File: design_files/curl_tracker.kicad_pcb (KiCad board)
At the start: 2 copper layers, 38 parts, among them J1 JST-PH, J2 USB_C_Receptacle, J3 SSD1306 OLED, J4 JST-PH, Q1 DMP2035, Q2 AO3400A, SW1 SW_Push, SW2 SW_Push, SW3 SW_Push, U1 AP2112K-3.3, U2 ESP32-C3-MINI-1, U3 MCP73831-2-OT, U4 BMI270, U5 USBLC6-2SC6

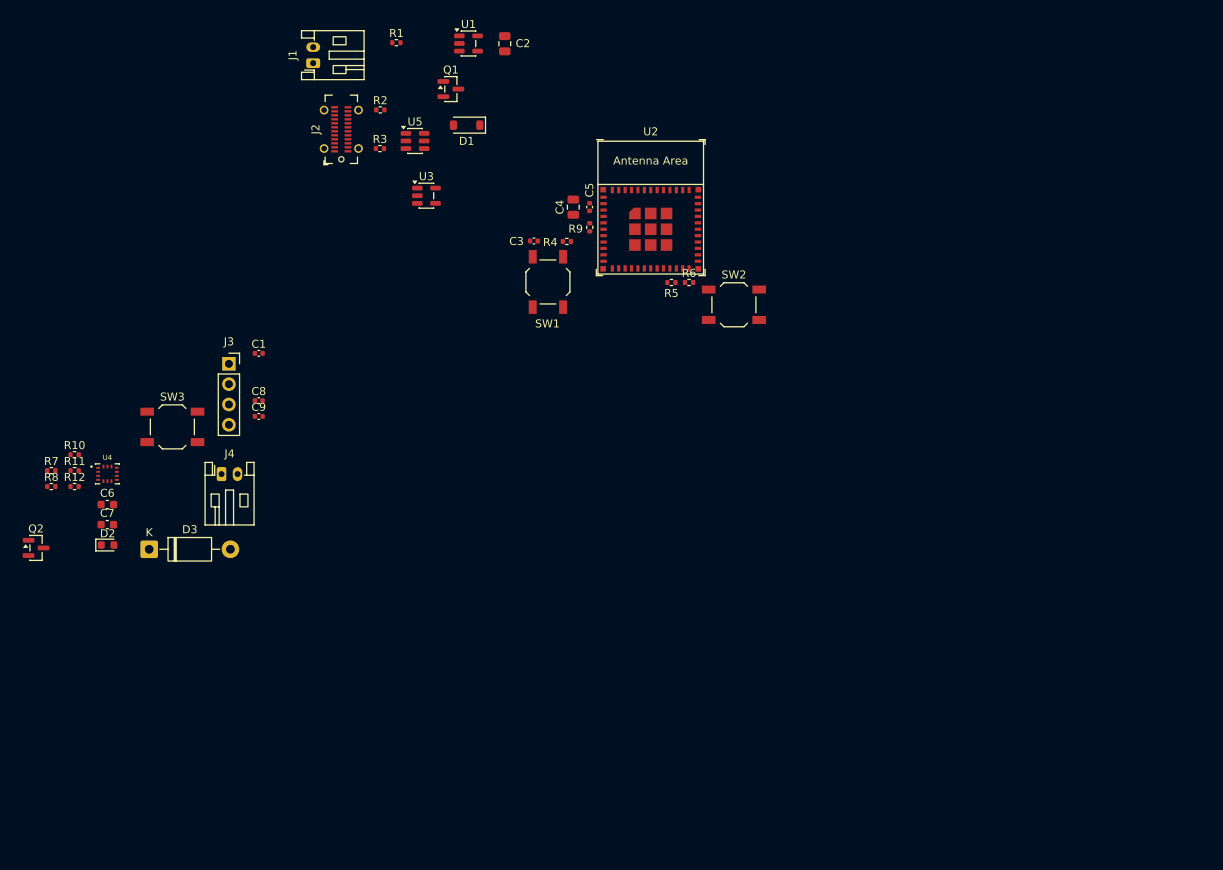
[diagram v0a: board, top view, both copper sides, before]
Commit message: start of esp-idf transition
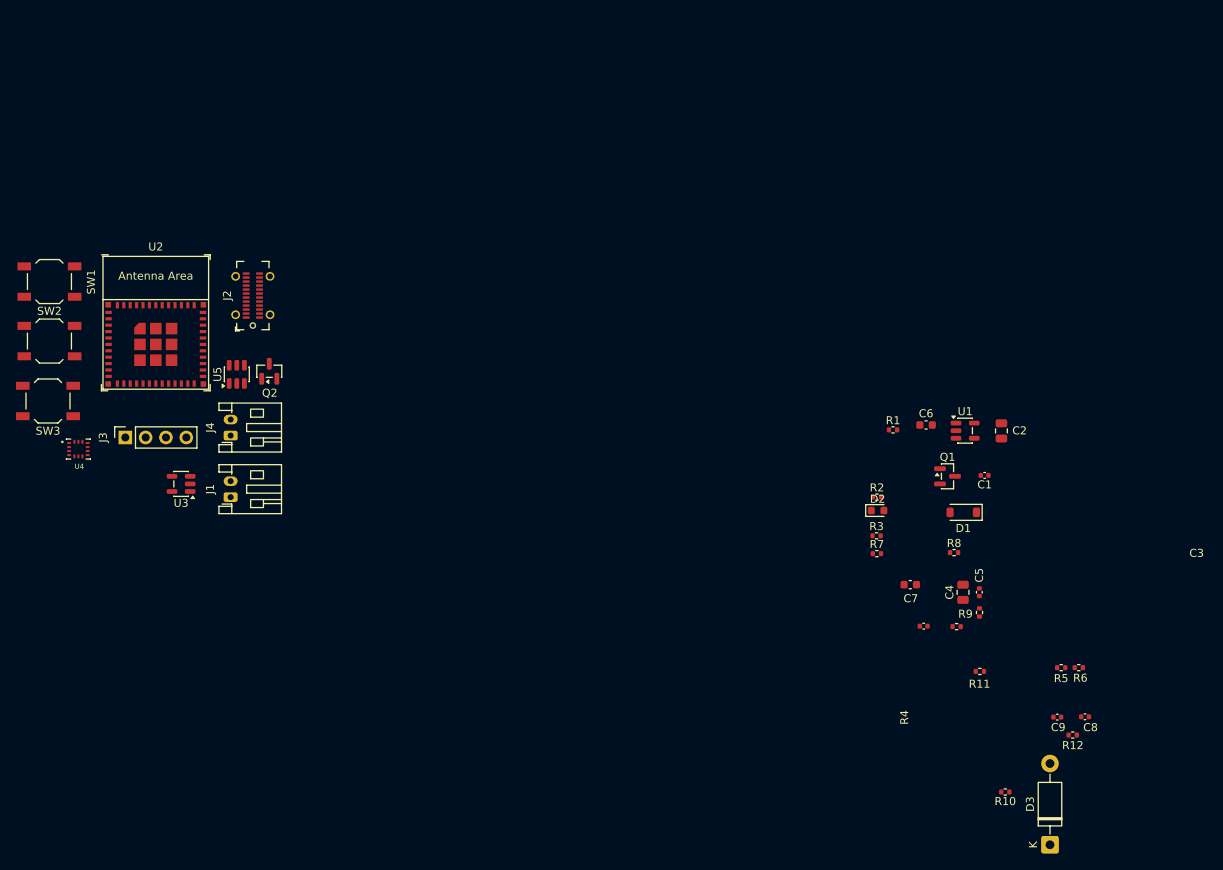
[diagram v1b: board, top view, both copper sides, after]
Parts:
- moved R12 128.6 mm to (255.7, 134.6)
- moved R10 123.7 mm to (247.2, 141.7), turned to 180 degrees
- moved D3 118.5 mm to (252.8, 148.3), turned to 90 degrees
- moved R11 115.9 mm to (244.0, 126.7)
- moved R8 113.1 mm to (240.8, 111.8)
- moved C8 110.6 mm to (257.2, 132.3), turned to 180 degrees
- moved C9 106.7 mm to (253.7, 132.4)
- moved R7 103.7 mm to (231.2, 111.9)
- moved C6 102.8 mm to (237.3, 95.9)
- moved C7 100.7 mm to (235.3, 115.8)
- moved D2 96.3 mm to (231.3, 106.5)
- moved C1 92.0 mm to (244.6, 102.2), turned to 180 degrees
- moved SW2 85.7 mm to (127.7, 85.4)
- moved D1 78.7 mm to (242.0, 106.8)
- moved Q1 78.7 mm to (240.0, 102.3)
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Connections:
- J3 pad 1: GND -> +3.3V
- J3 pad 2: +3.3V -> GND

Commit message: finished schematic
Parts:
- added C10: 4.7uF, Capacitor_SMD:C_0805_2012Metric, F.Cu at (158.7, 100.3)
- added C11: 4.7uF, Capacitor_SMD:C_0805_2012Metric, F.Cu at (163.1, 94.3)
- added C12: 100nF, Capacitor_SMD:C_0402_1005Metric, F.Cu at (140.3, 110.1)
- added C13: 100nF, Capacitor_SMD:C_0805_2012Metric, F.Cu at (163.1, 97.3)
- added C14: 100nF, Capacitor_SMD:C_0805_2012Metric, F.Cu at (163.1, 100.3)
- added C15: 100nF, Capacitor_SMD:C_0402_1005Metric, F.Cu at (140.3, 112.1)
- added L1: 2.2uH, Inductor_SMD:L_Coilcraft_LPS4018, F.Cu at (161.8, 118.7)
- added R13: 5.1k, Resistor_SMD:R_0402_1005Metric, F.Cu at (147.6, 103.7)
- added R14: 5.1k, Resistor_SMD:R_0402_1005Metric, F.Cu at (147.6, 105.7)
- added R15: 470, Resistor_SMD:R_0402_1005Metric, F.Cu at (150.5, 93.8)
- added R16: 5k, Resistor_SMD:R_0402_1005Metric, F.Cu at (150.5, 95.8)
- added R17: 10k, Resistor_SMD:R_0402_1005Metric, F.Cu at (150.5, 97.8)
- added R18: 100, Resistor_SMD:R_0402_1005Metric, F.Cu at (150.5, 99.7)
- added R19: 10k, Resistor_SMD:R_0402_1005Metric, F.Cu at (150.5, 101.7)
- C1, C3: value 1uF -> 10uF; footprint Capacitor_SMD:C_0402_1005Metric -> Capacitor_SMD:C_0805_2012Metric
- C5: value 100nF -> 1uF
- C6: value 4.7uF -> 100nF; footprint Capacitor_SMD:C_0603_1608Metric -> Capacitor_SMD:C_0402_1005Metric
- C7: value 4.7uF -> 10uF; footprint Capacitor_SMD:C_0603_1608Metric -> Capacitor_SMD:C_0805_2012Metric
- D3: footprint Diode_THT:D_DO-41_SOD81_P10.16mm_Horizontal -> Diode_SMD:D_SOD-123
- R10: value 100k -> 22
- R11: value 100 -> 10k
- R12, R6: value 4.7k -> 10k
- R2: value 5.1k -> 100
- R3: value 5.1k -> 100k
- R4: value 10k -> 100k
- R5: value 4.7k -> 100k
- R7: value 470 -> 4.7k
- R8: value 5k -> 4.7k
- R9: value 10k -> 22
- SW1, SW2, SW3: footprint Button_Switch_SMD:SW_SPST_TL3342 -> Button_Switch_SMD:SW_SPST_TL3305A
- U1: value AP2112K-3.3 -> TPS63001; footprint Package_TO_SOT_SMD:SOT-23-5 -> Package_SON:Texas_DRC0010J_ThermalVias
- moved C9 116.0 mm to (140.3, 108.1)
- moved R12 112.9 mm to (147.6, 101.7)
- moved R5 112.2 mm to (144.7, 101.7), turned to 0 degrees
- moved D3 110.5 mm to (146.2, 119.2), turned to 0 degrees
- moved R10 108.9 mm to (147.6, 97.8), turned to 0 degrees
- moved C5 104.7 mm to (140.3, 102.2), turned to 0 degrees
- moved R11 100.1 mm to (147.6, 99.7)
- moved R9 99.2 mm to (147.6, 95.8), turned to 0 degrees
- moved R4 98.8 mm to (144.7, 99.7)
- moved C6 97.4 mm to (140.3, 104.2)
- moved D1 96.2 mm to (146.2, 115.8), turned to 0 degrees
- moved R8 94.9 mm to (147.6, 93.8)
- moved C2 92.5 mm to (154.2, 97.3), turned to 0 degrees
- moved C1 90.8 mm to (154.2, 94.3), turned to 0 degrees
- moved R3 87.2 mm to (144.7, 97.8)
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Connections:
- net /INTR renamed /IO3
- C1 pad 1: Net-(D1-K) -> GND
- C1 pad 2: GND -> Net-(D1-K)
- C2 pad 1: +3.3V -> Net-(U1-EN)
- C3 pad 1: Net-(U2-EN/CHIP_PU) -> GND
- C3 pad 2: GND -> +3.3V
- C4 pad 1: +3.3V -> GND
- C4 pad 2: GND -> +3.3V
- C5 pad 1: +3.3V -> Net-(U2-EN/CHIP_PU)
- C6 pad 1: +5V -> Net-(U2-GPIO0/ADC1_CH0/XTAL_32K_P)
- C7 pad 1: VBATT -> +3.3V
- C9 pad 1: +3.3V -> GND
- C9 pad 2: GND -> +5V
- J3 pad 1: +3.3V -> GND
- J3 pad 2: GND -> +3.3V
- Q2 pad 2: Net-(D3-A) -> GND
- Q2 pad 3: GND -> Net-(D3-A)
- R10 pad 1: GND -> Net-(U2-GPIO7)
- R10 pad 2: Net-(Q2-G) -> /SDA
- R11 pad 1: Net-(Q2-G) -> Net-(U2-GPIO8)
- R11 pad 2: /GPIO4 -> +3.3V
- R12 pad 1: +3.3V -> Net-(U2-GPIO9)
- R12 pad 2: /GPIO5 -> +3.3V
- R2 pad 1: Net-(J2-CC1) -> Net-(D1-K)
- R2 pad 2: GND -> Net-(U1-EN)
- R3 pad 1: Net-(J2-CC2) -> +3.3V
- R3 pad 2: GND -> Net-(U2-EN/CHIP_PU)
- R4 pad 1: Net-(U2-EN/CHIP_PU) -> VBATT
- R4 pad 2: +3.3V -> Net-(U2-GPIO0/ADC1_CH0/XTAL_32K_P)
- R5 pad 1: /SDA -> Net-(U2-GPIO0/ADC1_CH0/XTAL_32K_P)
- R5 pad 2: +3.3V -> GND
- R6 pad 1: /SCL -> +3.3V
- R6 pad 2: +3.3V -> Net-(U2-GPIO2/ADC1_CH2)
- R7 pad 1: Net-(D2-K) -> +3.3V
- R7 pad 2: Net-(U3-STAT) -> Net-(U2-GPIO6)
- R8 pad 1: Net-(U3-PROG) -> +3.3V
- R8 pad 2: GND -> Net-(U2-GPIO7)
- R9 pad 1: +3.3V -> Net-(U2-GPIO6)
- R9 pad 2: Net-(U2-GPIO2/ADC1_CH2) -> /SCL
- SW2 pad 1: GND -> Net-(U2-GPIO9)
- SW2 pad 2: /SCL -> GND
- SW3 pad 2: /GPIO5 -> /IO5
- U1 pad 1: Net-(D1-K) -> +3.3V
- U1 pad 2: GND -> Net-(U1-L2)
- U1 pad 3: Net-(D1-K) -> GND
- U1 pad 4: unconnected-(U1-NC-Pad4) -> Net-(U1-L1)
- U1 pad 5: +3.3V -> Net-(D1-K)
- U2 pad 12: unconnected-(U2-GPIO0/ADC1_CH0/XTAL_32K_P-Pad12) -> Net-(U2-GPIO0/ADC1_CH0/XTAL_32K_P)
- U2 pad 18: /GPIO4 -> /IO4
- U2 pad 19: /GPIO5 -> /IO5
- U2 pad 20: unconnected-(U2-GPIO6-Pad20) -> Net-(U2-GPIO6)
- U2 pad 21: unconnected-(U2-GPIO7-Pad21) -> Net-(U2-GPIO7)
- U2 pad 22: /SDA -> Net-(U2-GPIO8)
- U2 pad 23: /SCL -> Net-(U2-GPIO9)
- U5 pad 4: /USB_P -> /USB_N
- U5 pad 6: /USB_N -> /USB_P
